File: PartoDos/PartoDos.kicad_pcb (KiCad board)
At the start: 2 copper layers, 80 x 100.2 mm, 60 parts, among them J1 RED4, J10 WHI4, J11 RED5, J12 GRE3, J13 GNC_BOND, J14 GNC_BOND, J15 GNC_BOND, J16 GNC_BOND, J17 GNC_BOND, J18 GNC_BOND, J19 GNC_BOND, J2 YEL4, J21 GNC_BOND, J23 GNC_BOND, J24 GNC_BOND, J25 GNC_BOND, J26 GNC_BOND, J27 TOP_STAR_VCC, J28 GNC_BOND, J29 GNC_BOND, J3 BLU1, J30 GNC_BOND, J31 GNC_BOND, J32 GNC_BOND, J33 GNC_BOND, J34 GNC_BOND, J4 YEL3, J5 GRE1, J6 WHI3, J7 GRE2, J8 BLU2, J9 YEL5

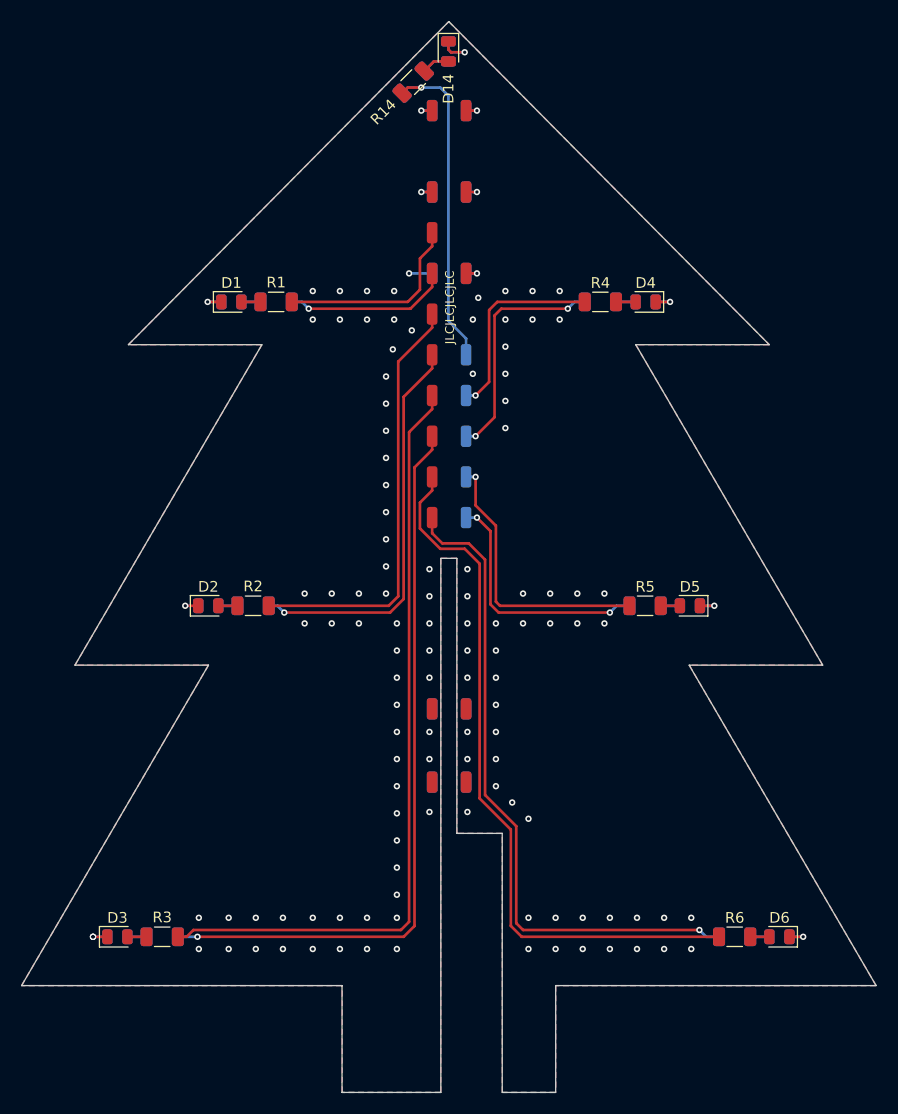
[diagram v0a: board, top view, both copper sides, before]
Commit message: Updated design
+ top LED
+ power switch
~ routing
~ via stitching more aligned
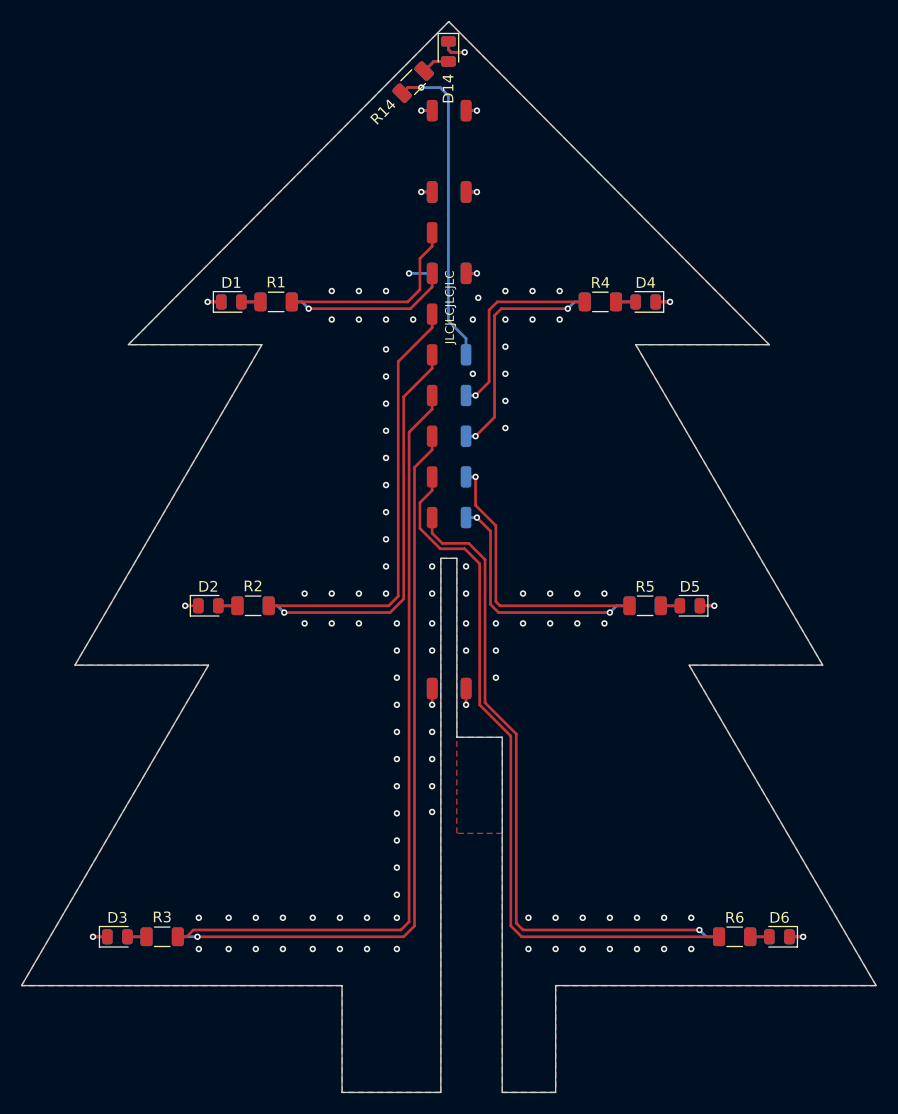
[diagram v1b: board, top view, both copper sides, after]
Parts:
- removed J29, J30, J31, J32, J33, J34: GNC_BOND, Connector_Wire:SolderWirePad_1x01_SMD_1x2mm
- added J20: GNC_BOND, Connector_Wire:SolderWirePad_1x01_SMD_1x2mm, F.Cu at (142.1, 115.2)
- added J22: GNC_BOND, Connector_Wire:SolderWirePad_1x01_SMD_1x2mm, B.Cu at (142.1, 115.2)
- J21: value GNC_BOND -> TOP_STAR_VCC
- J27: value TOP_STAR_VCC -> GNC_BOND
- moved J21 15.6 mm to (142.1, 83.9)
- moved J27 15.6 mm to (138.9, 68.7)
- moved J13 8.76 mm to (138.9, 115.2)
- moved J28 1.91 mm to (138.9, 115.2)
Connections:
- J21 pad 1: GND -> Net-(J21-Pad1)
- J27 pad 1: Net-(J27-Pad1) -> GND
- R13 pad 2: Net-(J27-Pad1) -> Net-(J21-Pad1)
- R14 pad 2: Net-(J27-Pad1) -> Net-(J21-Pad1)
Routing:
- net Net-(J27-Pad1): track 31.8 -> 0.00 mm, vias 1 -> 0
- net Net-(J21-Pad1): track 0.00 -> 31.8 mm, vias 0 -> 1
- net GND: track 31.6 -> 34.7 mm, vias 126 -> 115
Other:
- outline, holes or cut-outs redrawn
